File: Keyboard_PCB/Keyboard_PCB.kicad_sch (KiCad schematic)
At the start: 77 parts, among them J2 Conn_ARM_SWD_TagConnect_TC2030, J4 UART, SW1 BOOT, SW2 NRST, U1 S40FC002C1B2I00000, U2 STM32U385VGI6, U3 CC2500, U4 2450BM15B0003001E, Y1 26MHz, Y2 25MHz, Y3 32.786KHz

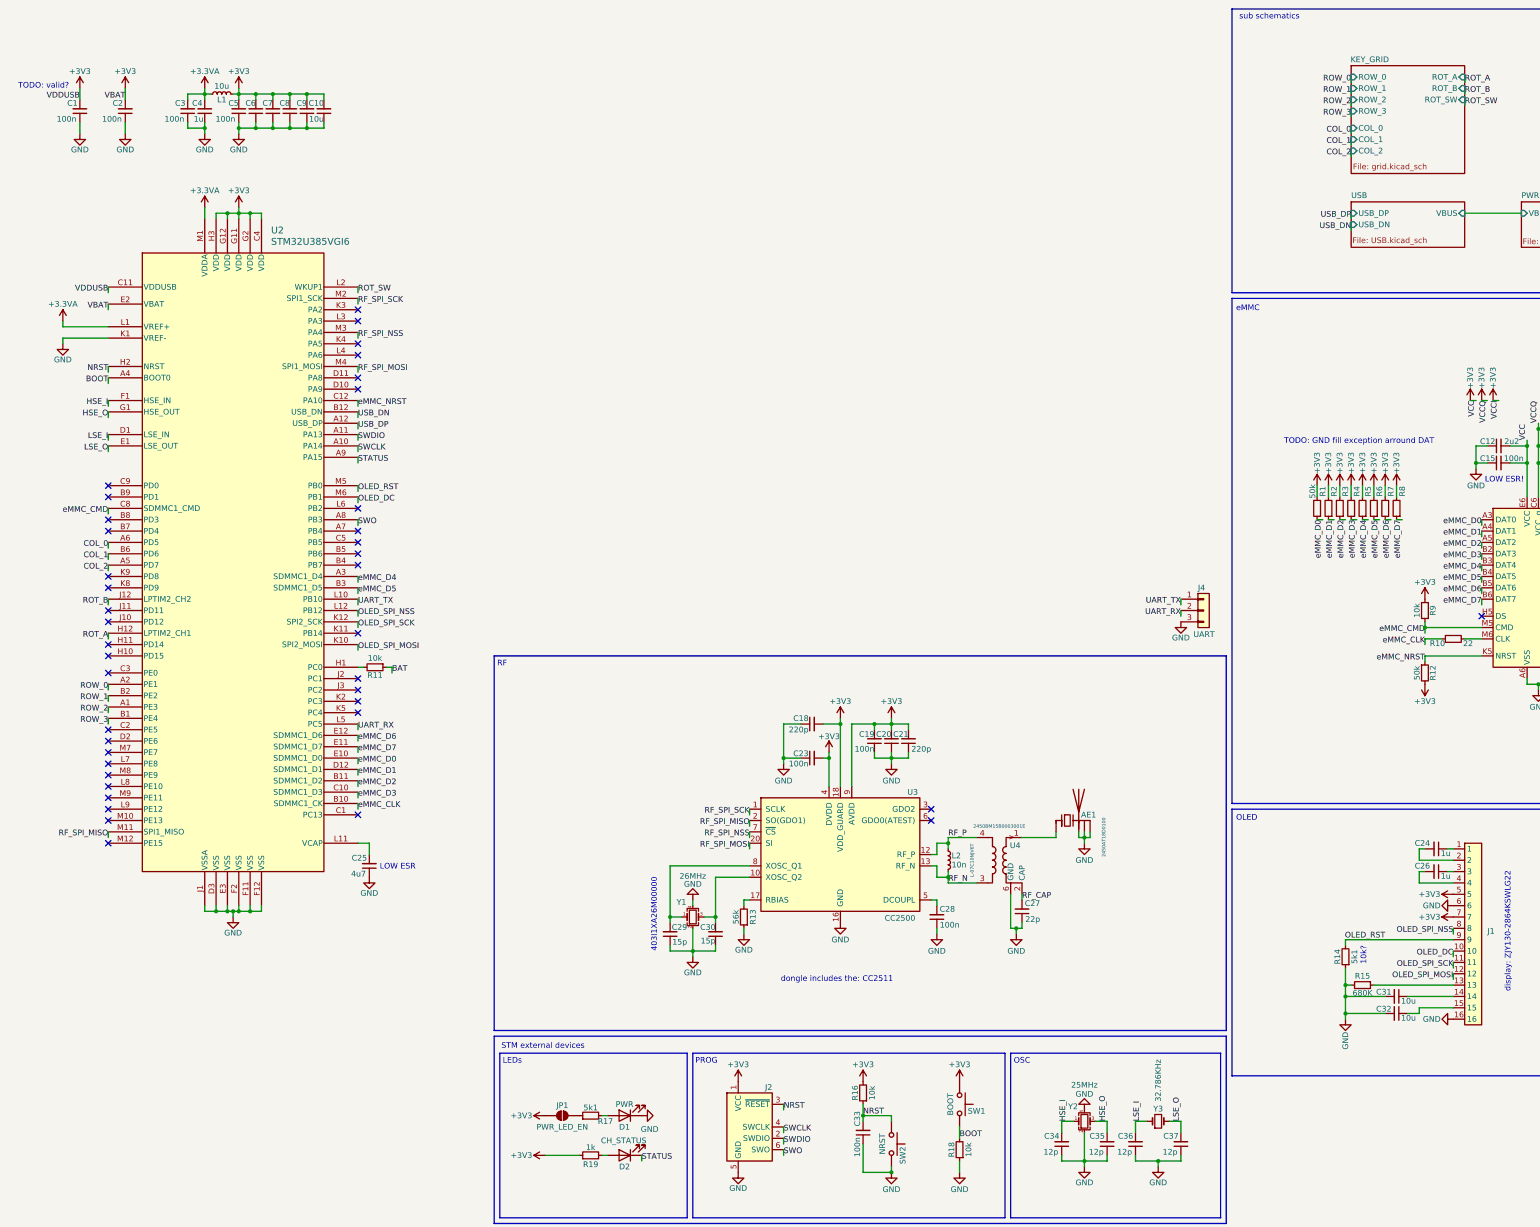
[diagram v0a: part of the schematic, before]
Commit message: Added mouser IDs to components and checked STM-eMMC connection
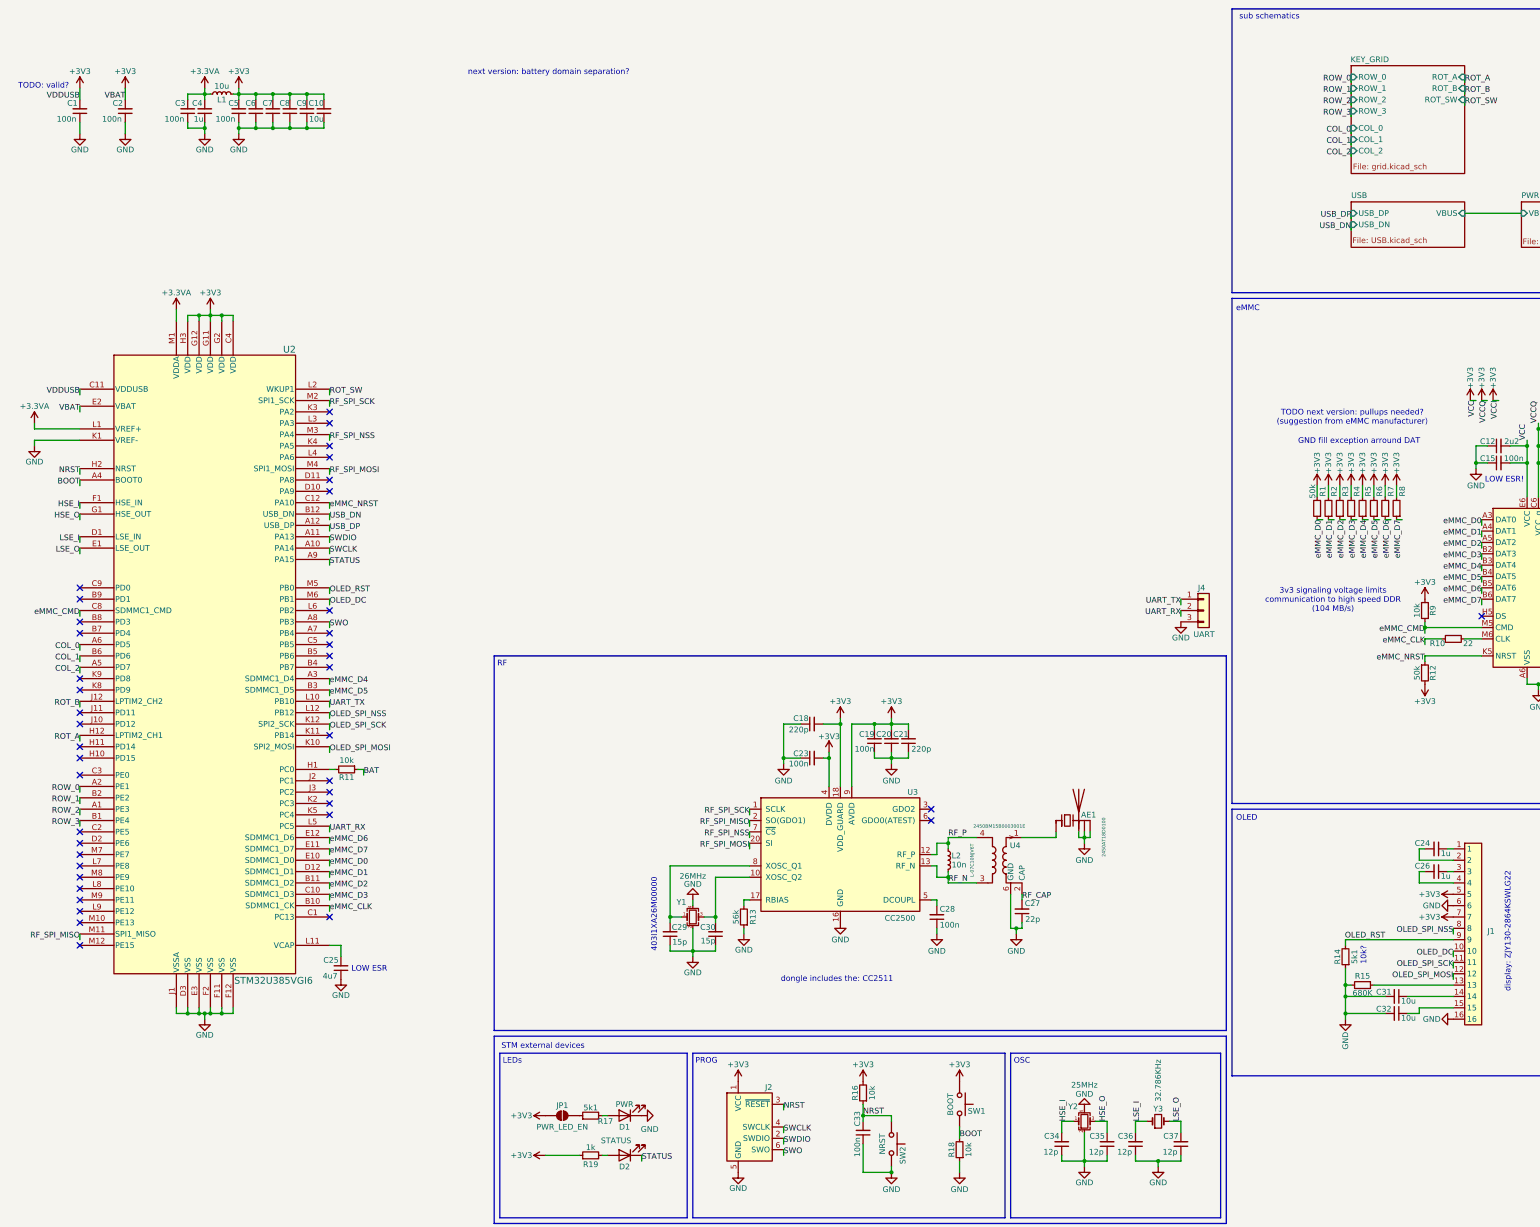
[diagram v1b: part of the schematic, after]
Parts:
- AE1: mouser (none) -> 609-2450AT18D0100001; now left out of the parts list
- C1, C11, C13, C15, C17, C2, C3, C4, C5, C6, C7, C8, C9: aliexpress (none) -> https://nl.aliexpress.com/item/1005002770949160.html?spm=a2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
- C10: mouser (none) -> 81-GRM155R60G106ME1D
- C12, C14, C16: mouser (none) -> 963-MSASL105SB5225MF
- C18, C19, C20, C21, C23, C24, C25, C26, C27, C28, C29, C30, C31, C32, C33, C34, C35, C36, C37, J4, L1, R11, R14, R15, R16, R17, R18, R19, SW1, SW2, Y2, Y3: now left out of the parts list
- D1: mouser 710-150060RS75000 -> (none); now left out of the parts list
- D2: value CH_STATUS -> STATUS; mouser 710-150060BS75000 -> (none); now left out of the parts list
- J1: mouser (none) -> 640-FFC2B28-16-G
- L2: mouser (none) -> 609-LRC0402CJ10NGV00
- R1, R10, R12, R2, R3, R4, R5, R6, R7, R8, R9: aliexpress (none) -> https://nl.aliexpress.com/item/1005002762720838.html?spm=a2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
- R13: mouser 791-RMC1/16-512JTP -> (none); now left out of the parts list
- U1: mouser (none) -> 727-0FC002C1B2I00000
- U2: mouser (none) -> 511-STM32U385VGI6
- U3: mouser (none) -> 595-CC2500RGP
- U4: mouser (none) -> 609-2450BM15B0003001
- Y1: mouser (none) -> 815-M826000MHZ10B1UT
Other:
- note added: "3v3 signaling voltage limits communication to high speed DDR (104 MB/s)"
- note added: "GND fill exception arround DAT"
- note added: "TODO next version: pullups needed? (suggestion from eMMC manufacturer)"
- note added: "next version: battery domain separation?"
- note removed: "TODO: GND fill exception arround DAT"
- moved on the sheet: C25, R11, U2

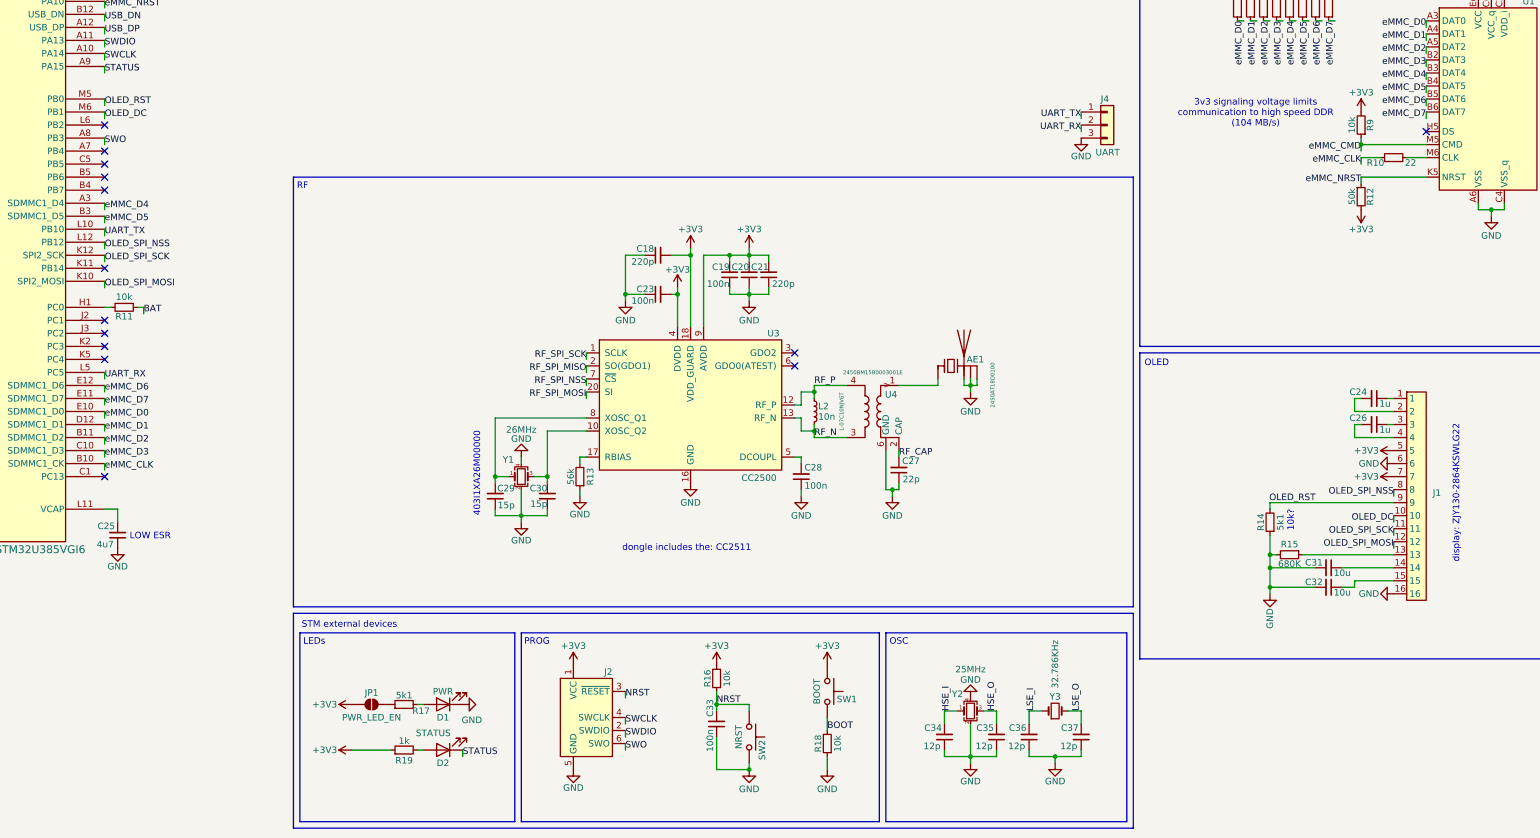
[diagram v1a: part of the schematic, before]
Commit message: Improved battery sens and added JLCPCB QR code
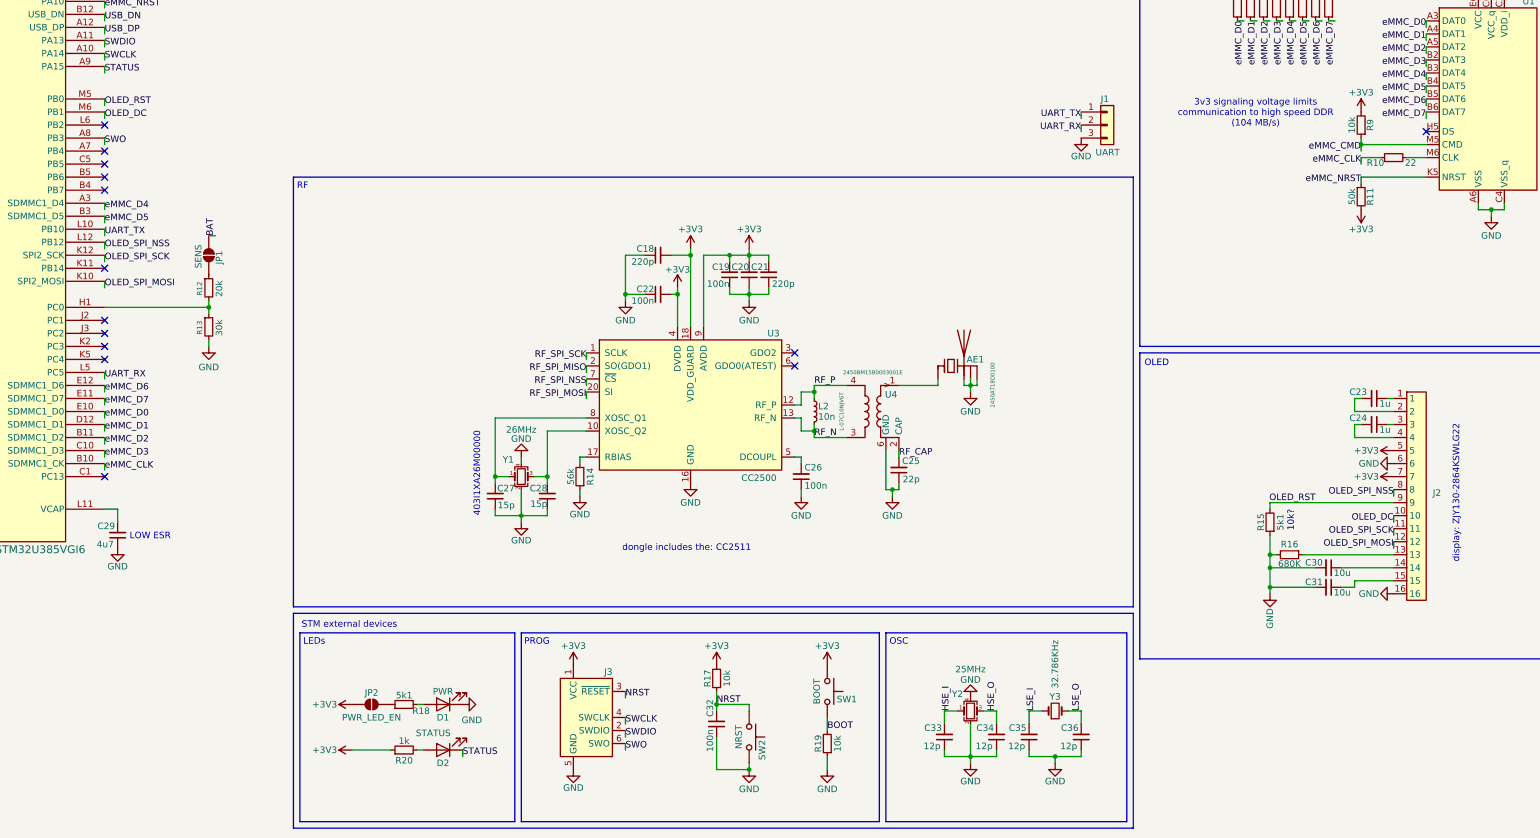
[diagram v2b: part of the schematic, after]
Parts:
- removed R11: 10k, Resistor_SMD:R_0603_1608Metric, symbol Device:R_Small
- added JP1: SENS, Jumper:SolderJumper-2_P1.3mm_Open_TrianglePad1.0x1.5mm, symbol Jumper:SolderJumper_2_Open
- added R12: 20k, Resistor_SMD:R_0603_1608Metric, symbol Device:R_Small
- added R13: 30k, Resistor_SMD:R_0603_1608Metric, symbol Device:R_Small
- renumbered C23 to C22, C24 to C23, C26 to C24, C27 to C25, C28 to C26, C29 to C27, C30 to C28, C25 to C29, C31 to C30, C32 to C31, C33 to C32, C34 to C33, C35 to C34, C36 to C35, C37 to C36, J4 to J1, J1 to J2, J2 to J3, JP1 to JP2, R12 to R11, R13 to R14, R14 to R15, R15 to R16, R16 to R17, R17 to R18, R18 to R19, R19 to R20
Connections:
- net BAT: now also JP1.1 (A)
- net GND: now also R13.2
- net at U2.H1 (PC0): now also R12.2, R13.1
- new net: JP1.2 (B), R12.1

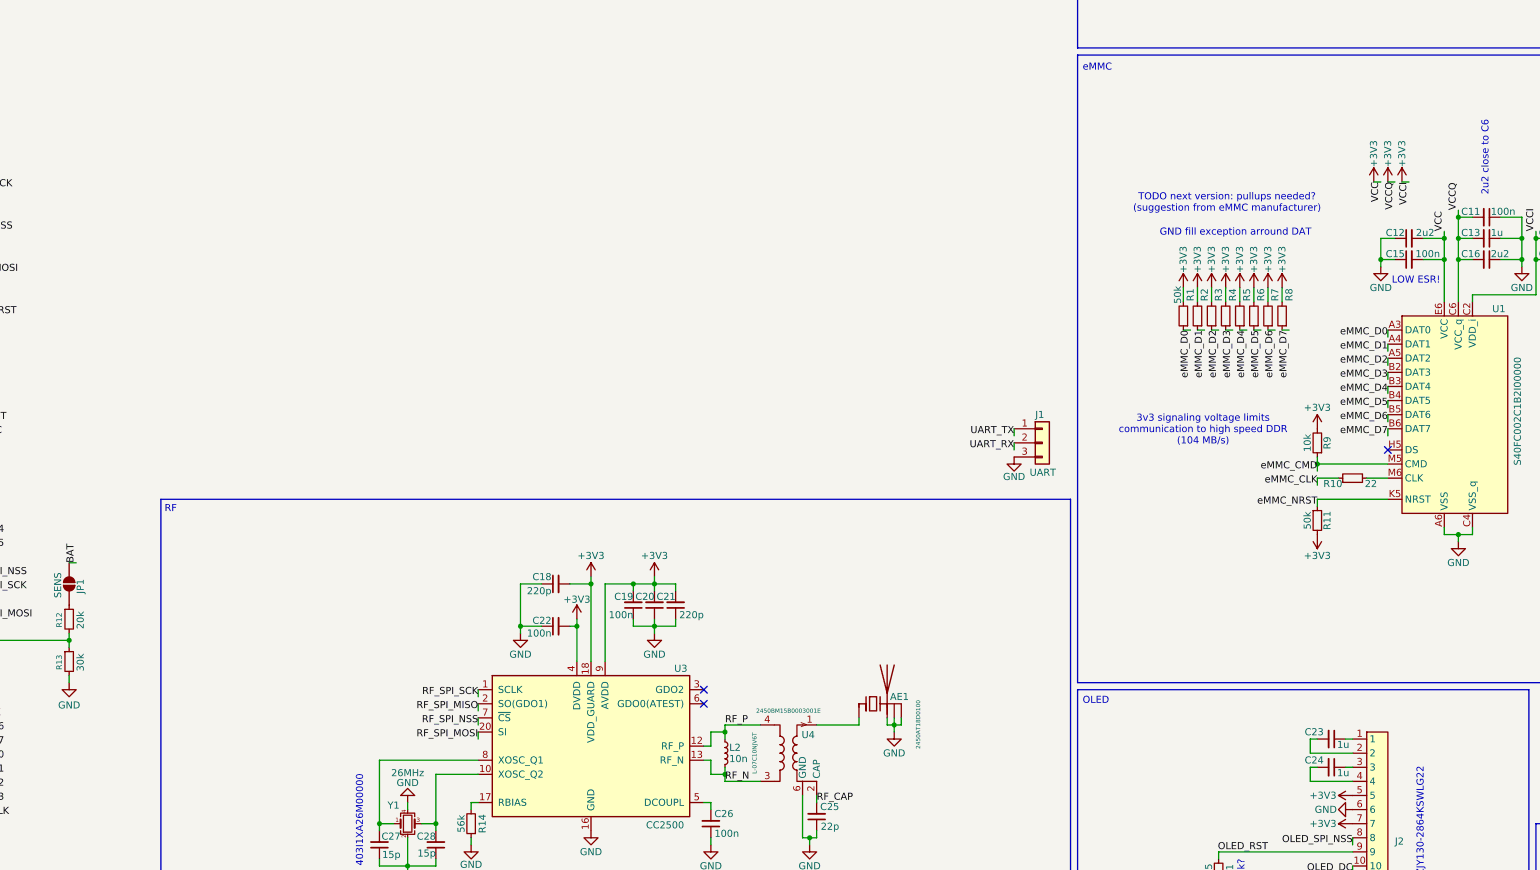
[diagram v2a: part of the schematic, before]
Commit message: Added TODOs for next version
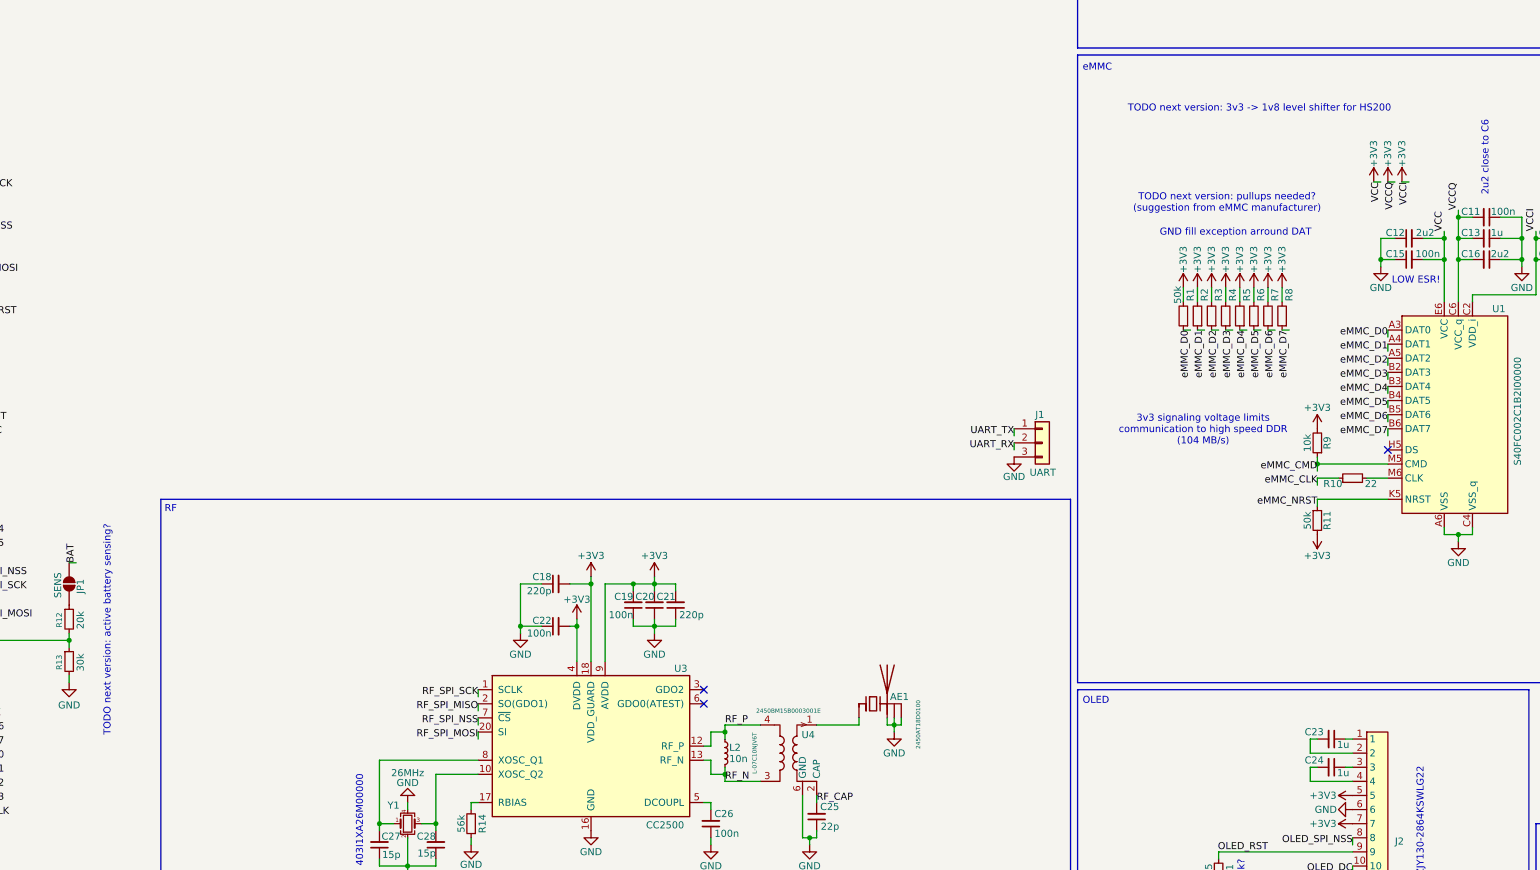
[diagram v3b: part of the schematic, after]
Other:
- note added: "TODO next version: 3v3 -> 1v8 level shifter for HS200"
- note added: "TODO next version: active battery sensing?"
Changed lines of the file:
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@@
+		)
+	)
+	(text "TODO next version: active battery sensing?"
+		(exclude_from_sim no)
+		(at 126.238 181.102 90)
+		(effects
+			(font
+				(size 1.27 1.27)
+			)
+		)
+	)
+	(text "TODO next version: 3v3 -> 1v8 level shifter for HS200"
+		(exclude_from_sim no)
+		(at 333.756 87.122 0)
+		(effects
+			(font
+				(size 1.27 1.27)
+			)
 		)
 	)
